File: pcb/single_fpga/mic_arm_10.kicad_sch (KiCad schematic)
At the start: 17 parts, among them U109 CDCLVC1108PW, U81 IM72D128V01XTMA1, U82 IM72D128V01XTMA1, U83 IM72D128V01XTMA1, U84 IM72D128V01XTMA1, U85 IM72D128V01XTMA1, U86 IM72D128V01XTMA1, U87 IM72D128V01XTMA1, U88 IM72D128V01XTMA1

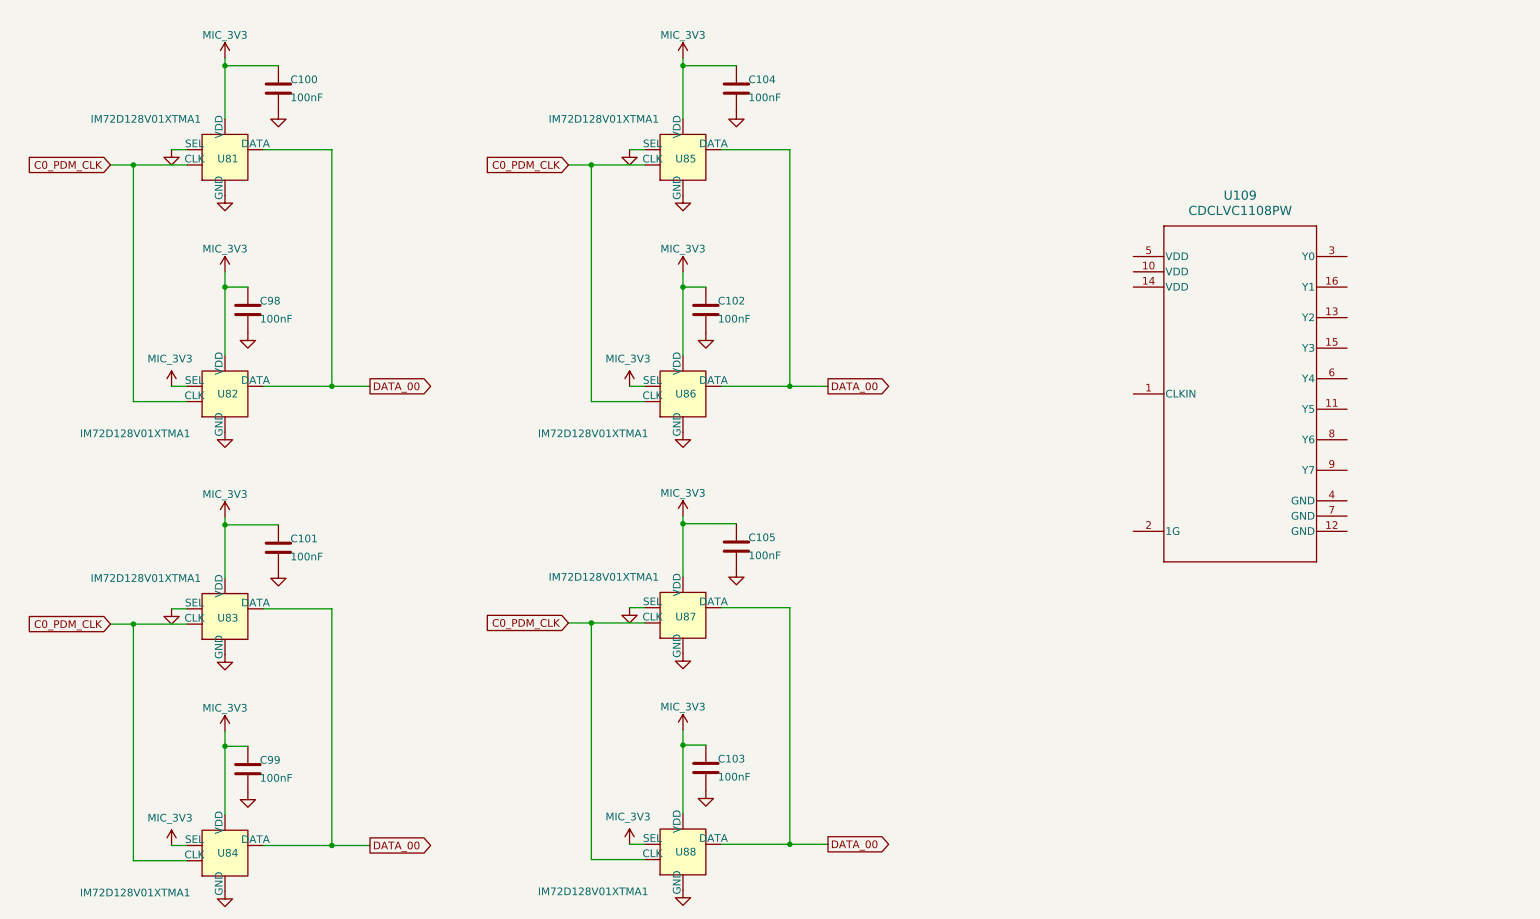
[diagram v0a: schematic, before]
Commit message: Fixed clocks and names.
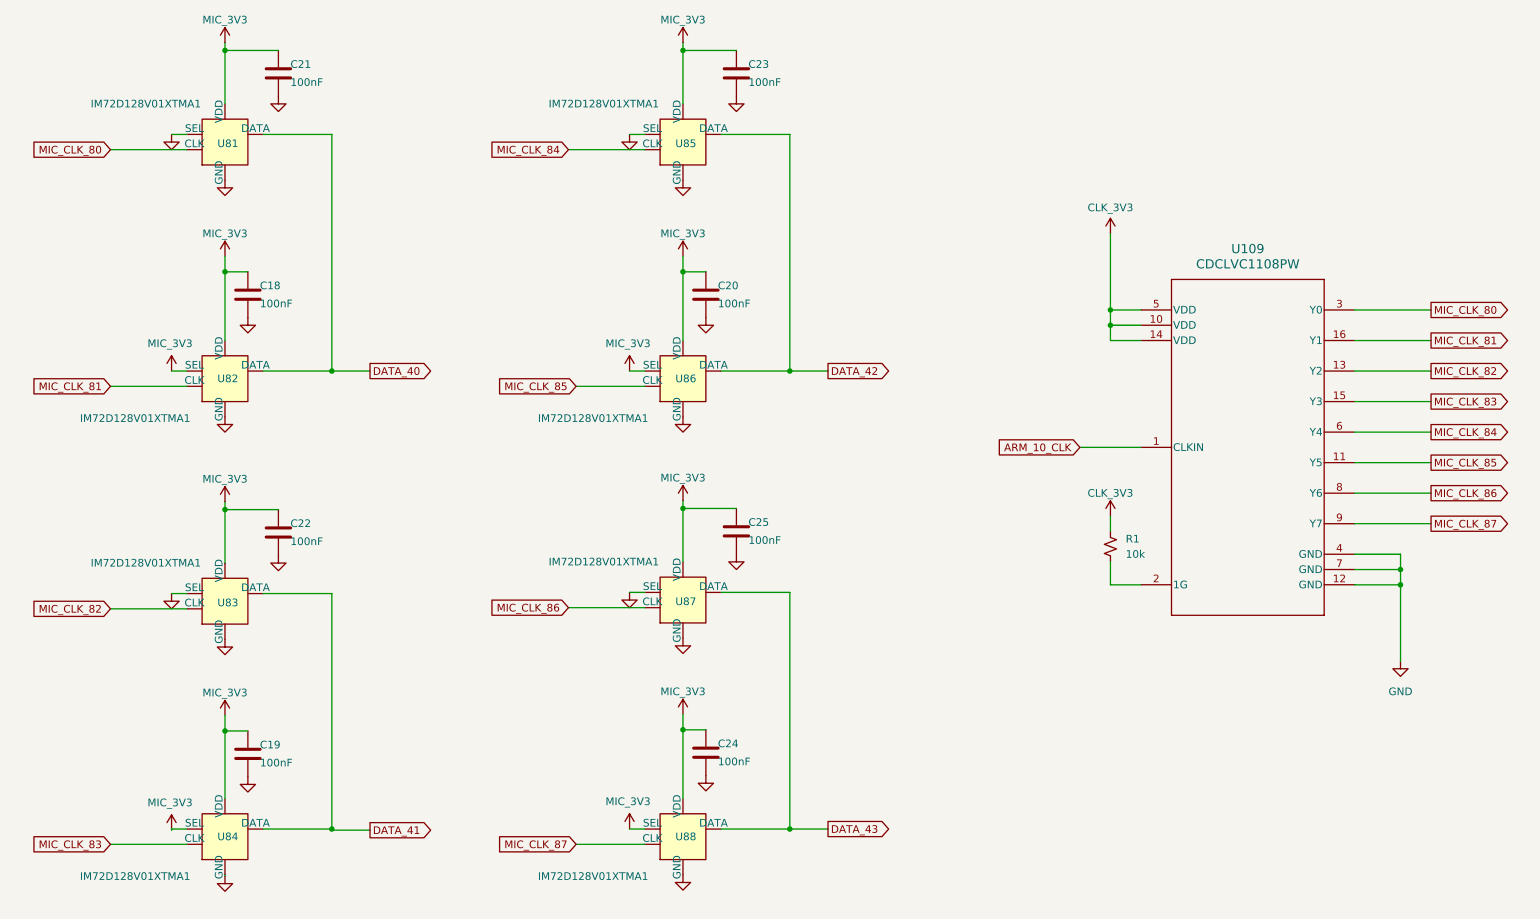
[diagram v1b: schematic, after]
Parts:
- removed C100, C101, C102, C103, C104, C105, C98, C99: 100nF, Capacitor_SMD:C_0603_1608Metric, symbol Device:C
- added C18, C19, C20, C21, C22, C23, C24, C25: 100nF, Capacitor_SMD:C_0603_1608Metric, symbol Device:C
- added R1: 10k, PCM_SparkFun-Resistor:R_0603_1608Metric, symbol PCM_SparkFun-Resistor:10k_0603
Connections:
- net GND: now also U109.12 (GND), U109.4 (GND), U109.7 (GND), C18.2, C19.2, C20.2, C21.2, C22.2, C23.2, C24.2, C25.2
- net MIC_3V3: now also C18.1, C19.1, C20.1, C21.1, C22.1, C23.1, C24.1, C25.1
- net ARM_10_CLK: now reaches U109.1 (CLKIN)
- net CLK_3V3: now reaches U109.10 (VDD)
- net CLK_3V3: now also U109.14 (VDD), U109.5 (VDD), R1.2
- net MIC_CLK_85: now reaches U109.11 (Y5)
- net MIC_CLK_85: now also U86.3 (CLK)
- net MIC_CLK_82: now reaches U109.13 (Y2)
- net MIC_CLK_82: now also U83.3 (CLK)
- net MIC_CLK_83: now reaches U109.15 (Y3)
- net MIC_CLK_83: now also U84.3 (CLK)
- net MIC_CLK_81: now reaches U109.16 (Y1)
- net MIC_CLK_81: now also U82.3 (CLK)
- net at U109.2 (1G): now also R1.1
- net MIC_CLK_80: now reaches U109.3 (Y0)
- net MIC_CLK_80: now also U81.3 (CLK)
- net MIC_CLK_84: now reaches U109.6 (Y4)
- net MIC_CLK_84: now also U85.3 (CLK)
- net MIC_CLK_86: now reaches U109.8 (Y6)
- net MIC_CLK_86: now also U87.3 (CLK)
- net MIC_CLK_87: now reaches U109.9 (Y7)
- net MIC_CLK_87: now also U88.3 (CLK)
- removed net C0_PDM_CLK: U81.3 (CLK), U82.3 (CLK), U83.3 (CLK), U84.3 (CLK), U85.3 (CLK), U86.3 (CLK), U87.3 (CLK), U88.3 (CLK)
- removed net DATA_00: U81.1 (DATA), U82.1 (DATA), U83.1 (DATA), U84.1 (DATA), U85.1 (DATA), U86.1 (DATA), U87.1 (DATA), U88.1 (DATA)
- new net DATA_40: U81.1 (DATA), U82.1 (DATA)
- new net DATA_41: U83.1 (DATA), U84.1 (DATA)
- new net DATA_42: U85.1 (DATA), U86.1 (DATA)
- new net DATA_43: U87.1 (DATA), U88.1 (DATA)

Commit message: Fixed all duplicate refdes's.
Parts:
- renumbered C20 to C100, C21 to C101, C22 to C102, C23 to C103, C24 to C104, C25 to C105, C18 to C98, C19 to C99, R1 to R15

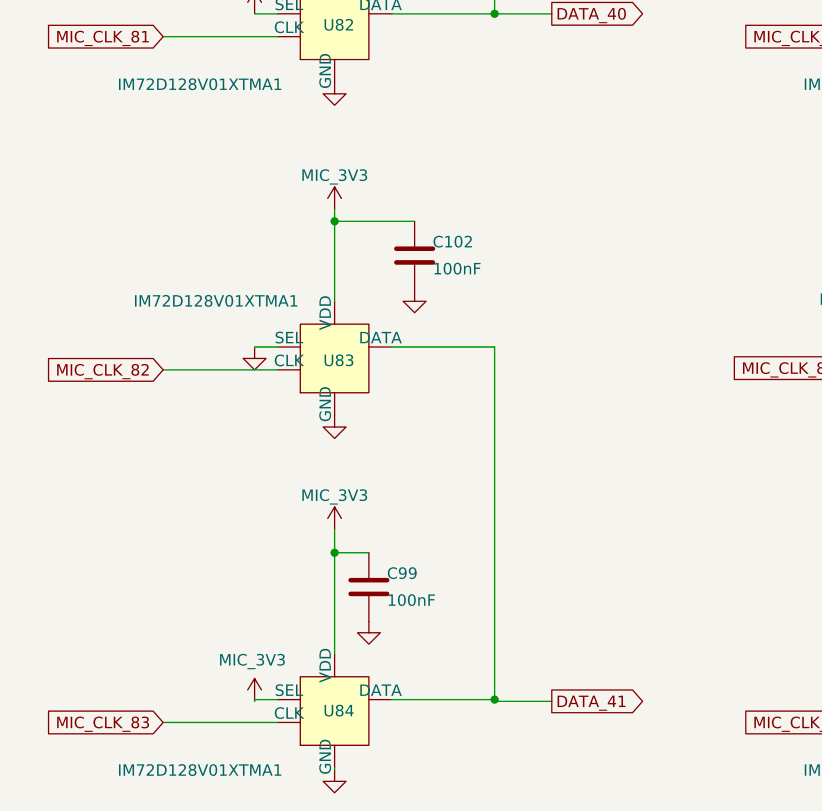
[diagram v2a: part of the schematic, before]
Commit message: Fixed symbol library references.
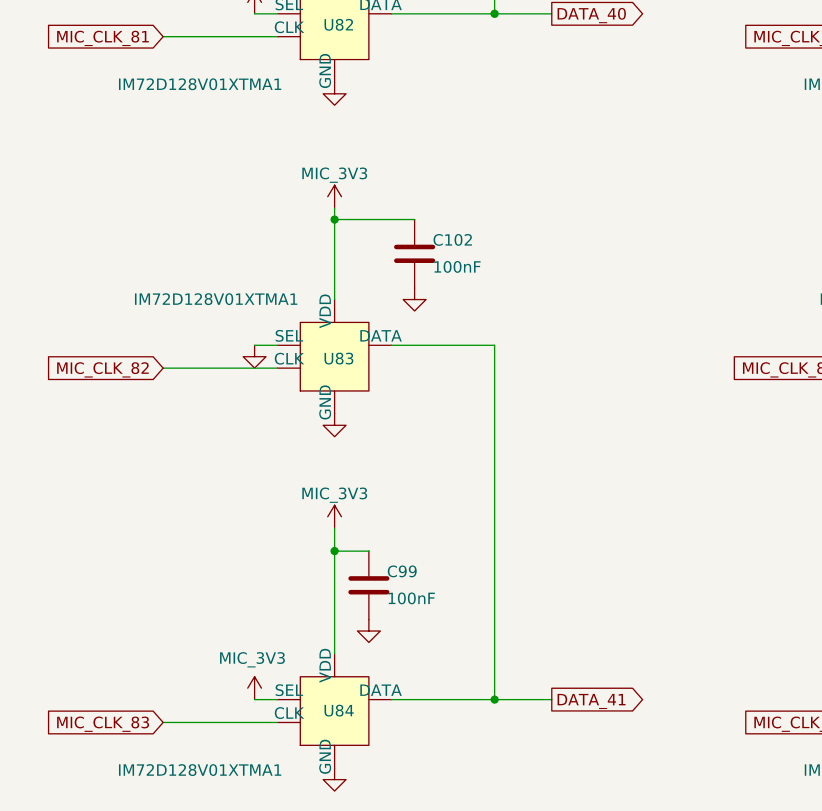
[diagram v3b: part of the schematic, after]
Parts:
- U109: footprint PW0016A_N -> CDCLVC1108:PW0016A_N

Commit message: Fixed footprints. Added missing mic. Relinked placed footprints.
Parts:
- U81, U82, U83, U84, U85, U86, U87, U88: footprint (none) -> IM72D128:IFX-PG-LLGA-5-4
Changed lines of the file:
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@@
 			)
 		)
-		(property "Footprint" ""
+		(property "Footprint" "IM72D128:IFX-PG-LLGA-5-4"
 			(at 59.69 160.02 0)
 			(hide yes)
@@
 			)
 		)
-		(property "Footprint" ""
+		(property "Footprint" "IM72D128:IFX-PG-LLGA-5-4"
 			(at 135.89 160.02 0)
 			(hide yes)
@@
 			)
 		)
-		(property "Footprint" ""
+		(property "Footprint" "IM72D128:IFX-PG-LLGA-5-4"
 			(at 59.69 83.82 0)
 			(hide yes)
@@
 			)
 		)
-		(property "Footprint" ""
+		(property "Footprint" "IM72D128:IFX-PG-LLGA-5-4"
 			(at 59.69 120.65 0)
 			(hide yes)
@@
 			)
 		)
-		(property "Footprint" ""
+		(property "Footprint" "IM72D128:IFX-PG-LLGA-5-4"
 			(at 59.69 44.45 0)
 			(hide yes)
@@
 			)
 		)
-		(property "Footprint" ""
+		(property "Footprint" "IM72D128:IFX-PG-LLGA-5-4"
 			(at 135.89 83.82 0)
 			(hide yes)
@@
 			)
 		)
-		(property "Footprint" ""
+		(property "Footprint" "IM72D128:IFX-PG-LLGA-5-4"
 			(at 135.89 44.45 0)
 			(hide yes)
@@
 			)
 		)
-		(property "Footprint" ""
+		(property "Footprint" "IM72D128:IFX-PG-LLGA-5-4"
 			(at 135.89 120.65 0)
 			(hide yes)

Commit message: Updated all refdes's.
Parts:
- removed C100, C101, C102, C103, C104, C105, C98, C99: 100nF, Capacitor_SMD:C_0603_1608Metric, symbol Device:C
- removed R15: 10k, PCM_SparkFun-Resistor:R_0603_1608Metric, symbol PCM_SparkFun-Resistor:10k_0603
- removed U109: CDCLVC1108PW, CDCLVC1108:PW0016A_N, symbol CDCLVC1108:CDCLVC1108PW
- removed U81, U82, U83, U84, U85, U86, U87, U88: IM72D128V01XTMA1, IM72D128:IFX-PG-LLGA-5-4, symbol multi_fpga:IM72D128
- added C81, C82, C83, C84, C85, C86, C87, C88: 100nF, Capacitor_SMD:C_0603_1608Metric, symbol Device:C
- added R11: 10k, PCM_SparkFun-Resistor:R_0603_1608Metric, symbol PCM_SparkFun-Resistor:10k_0603
- added U91, U92, U93, U94, U95, U96, U97, U98: IM72D128V01XTMA1, IM72D128:IFX-PG-LLGA-5-4, symbol multi_fpga:IM72D128
- added U99: CDCLVC1108PW, CDCLVC1108:PW0016A_N, symbol CDCLVC1108:CDCLVC1108PW
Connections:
- net ARM_10_CLK: now also U99.1 (CLKIN)
- net CLK_3V3: now also R11.2, U99.10 (VDD), U99.14 (VDD), U99.5 (VDD)
- net DATA_40: now also U91.1 (DATA), U92.1 (DATA)
- net DATA_41: now also U93.1 (DATA), U94.1 (DATA)
- net DATA_42: now also U95.1 (DATA), U96.1 (DATA)
- net DATA_43: now also U97.1 (DATA), U98.1 (DATA)
- net GND: now also C81.2, C82.2, C83.2, C84.2, C85.2, C86.2, C87.2, C88.2, U91.4 (SEL), U91.5 (GND), U92.5 (GND), U93.4 (SEL), U93.5 (GND), U94.5 (GND), U95.4 (SEL), U95.5 (GND), U96.5 (GND), U97.4 (SEL), U97.5 (GND), U98.5 (GND), U99.12 (GND), U99.4 (GND), U99.7 (GND)
- net MIC_3V3: now also C81.1, C82.1, C83.1, C84.1, C85.1, C86.1, C87.1, C88.1, U91.2 (VDD), U92.2 (VDD), U92.4 (SEL), U93.2 (VDD), U94.2 (VDD), U94.4 (SEL), U95.2 (VDD), U96.2 (VDD), U96.4 (SEL), U97.2 (VDD), U98.2 (VDD), U98.4 (SEL)
- net MIC_CLK_80: now also U91.3 (CLK), U99.3 (Y0)
- net MIC_CLK_81: now also U92.3 (CLK), U99.16 (Y1)
- net MIC_CLK_82: now also U93.3 (CLK), U99.13 (Y2)
- net MIC_CLK_83: now also U94.3 (CLK), U99.15 (Y3)
- net MIC_CLK_84: now also U95.3 (CLK), U99.6 (Y4)
- net MIC_CLK_85: now also U96.3 (CLK), U99.11 (Y5)
- net MIC_CLK_86: now also U97.3 (CLK), U99.8 (Y6)
- net MIC_CLK_87: now also U98.3 (CLK), U99.9 (Y7)
- new net: R11.1, U99.2 (1G)
